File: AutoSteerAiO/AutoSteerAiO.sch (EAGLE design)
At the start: 82 parts, among them J4 CONNECTOR 1x5 PINS, K4 CB1A-P-12V, U1 VX7805-1000

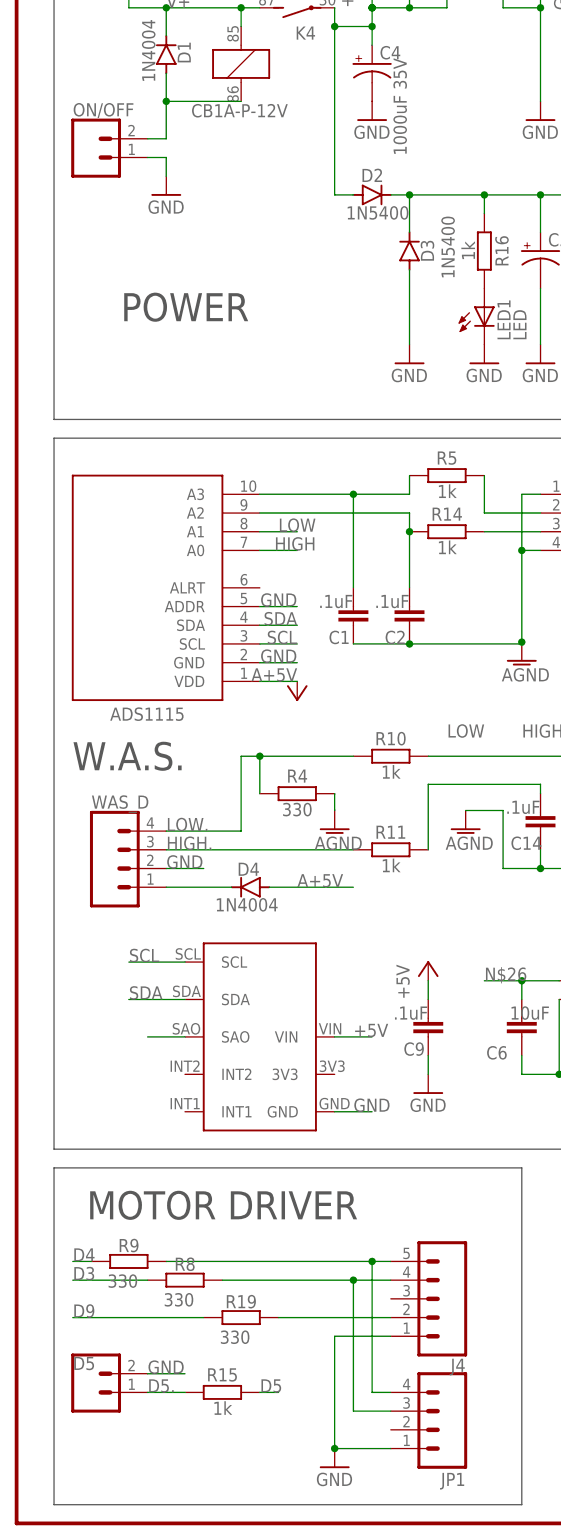
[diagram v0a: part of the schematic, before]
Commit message: Add files via upload
added led autosteer
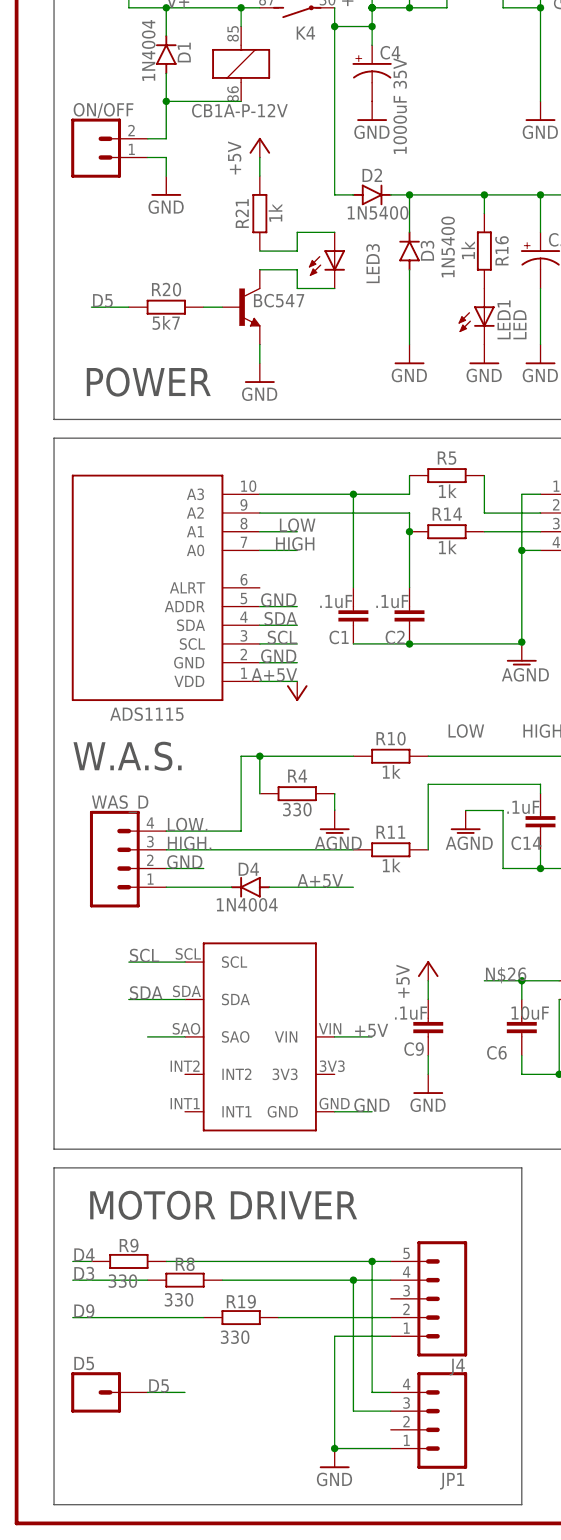
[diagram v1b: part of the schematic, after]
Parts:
- removed R15: 1k, resistor:R-EU_0207/7
- added LED3: LED, adafruit:LED5MM
- added R20: 5k7, resistor:R-EU_0207/7
- added R21: 1k, resistor:R-EU_0207/7
- added T1: BC547, transistor:BC547
- D5: device SparkFun-Connectors:CONN_02 -> SparkFun-Connectors:CONN_01
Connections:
- removed net D5.: D5.1, R15.1
- new net N$23: R20.2, T1.B
- new net N$24: LED3.A, R21.1
- new net N$27: LED3.C, T1.C
- net +5V: now also R21.2
- net D5: now also D5.1, R20.1; no longer R15.2
- net GND: now also T1.E; no longer D5.2
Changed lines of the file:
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@@
 <attribute name="OC_NEWARK" value="unknown"/>
 </part>
-<part name="D5" library="SparkFun-Connectors" library_urn="urn:adsk.eagle:library:513" deviceset="CONN_02" device="" package3d_urn="urn:adsk.eagle:package:38039/1" value="CONNECTOR 1x1 PIN">
+<part name="D5" library="SparkFun-Connectors" library_urn="urn:adsk.eagle:library:513" deviceset="CONN_01" device="" package3d_urn="urn:adsk.eagle:package:38028/1" value="CONNECTOR 1x1 PIN">
 <attribute name="MF" value=""/>
 <attribute name="MPN" value=""/>
@@
 </part>
 <part name="U$13" library="#MMA8542Q" deviceset="MMA8542Q" device=""/>
-<part name="R15" library="resistor" library_urn="urn:adsk.eagle:library:348" deviceset="R-EU_" device="0207/7" package3d_urn="urn:adsk.eagle:package:23493/2" value="1k">
+<part name="T1" library="transistor" library_urn="urn:adsk.eagle:library:402" deviceset="BC547" device="" package3d_urn="urn:adsk.eagle:package:28523/2"/>
+<part name="R20" library="resistor" library_urn="urn:adsk.eagle:library:348" deviceset="R-EU_" device="0207/7" package3d_urn="urn:adsk.eagle:package:23493/2" value="5k7">
+<attribute name="MF" value=""/>
+<attribute name="MPN" value=""/>
+<attribute name="OC_NEWARK" value="unknown"/>
+</part>
+<part name="R21" library="resistor" library_urn="urn:adsk.eagle:library:348" deviceset="R-EU_" device="0207/7" package3d_urn="urn:adsk.eagle:package:23493/2" value="1k">
+<attribute name="MF" value=""/>
+<attribute name="MPN" value=""/>
+<attribute name="OC_NEWARK" value="unknown"/>
+</part>
+<part name="P+3" library="supply1" library_urn="urn:adsk.eagle:library:371" deviceset="+5V" device=""/>
+<part name="GND11" library="supply1" library_urn="urn:adsk.eagle:library:371" deviceset="GND" device=""/>
+<part name="LED3" library="adafruit" library_urn="urn:adsk.eagle:library:420" deviceset="LED" device="5MM" package3d_urn="urn:adsk.eagle:package:6240538/1" value="LED">
 <attribute name="MF" value=""/>
 <attribute name="MPN" value=""/>
@@
 <wire x1="144.78" y1="213.36" x2="144.78" y2="284.48" width="0.1524" layer="97"/>
 <wire x1="144.78" y1="213.36" x2="5.08" y2="213.36" width="0.1524" layer="97"/>
-<text x="22.86" y="228.6" size="3.81" layer="97" font="vector" align="center">POWER</text>
+<text x="17.78" y="218.44" size="3.81" layer="97" font="vector" align="center">POWER</text>
 <wire x1="147.32" y1="198.12" x2="147.32" y2="256.54" width="0.1524" layer="97"/>
 <wire x1="205.74" y1="198.12" x2="147.32" y2="198.12" width="0.1524" layer="97"/>
@@
 </instance>
 <instance part="U$13" gate="G$1" x="86.36" y="149.86" smashed="yes"/>
-<instance part="R15" gate="G$1" x="27.94" y="81.28" smashed="yes">
-<attribute name="NAME" x="27.94" y="82.7786" size="1.778" layer="95" rot="R180" align="top-center"/>
-<attribute name="VALUE" x="27.94" y="80.01" size="1.778" layer="95" rot="R180" align="bottom-center"/>
-<attribute name="OC_NEWARK" x="27.94" y="81.28" size="1.778" layer="96" display="off"/>
-<attribute name="MF" x="27.94" y="81.28" size="1.778" layer="96" display="off"/>
-<attribute name="MPN" x="27.94" y="81.28" size="1.778" layer="96" display="off"/>
+<instance part="T1" gate="G$1" x="30.48" y="228.6" smashed="yes">
+<attribute name="VALUE" x="32.004" y="228.6" size="1.778" layer="96"/>
+</instance>
+<instance part="R20" gate="G$1" x="20.32" y="228.6" smashed="yes">
+<attribute name="NAME" x="20.32" y="230.0986" size="1.778" layer="95" rot="R180" align="top-center"/>
+<attribute name="VALUE" x="20.32" y="227.33" size="1.778" layer="95" rot="R180" align="bottom-center"/>
+<attribute name="OC_NEWARK" x="20.32" y="228.6" size="1.778" layer="96" display="off"/>
+<attribute name="MF" x="20.32" y="228.6" size="1.778" layer="96" display="off"/>
+<attribute name="MPN" x="20.32" y="228.6" size="1.778" layer="96" display="off"/>
+</instance>
+<instance part="R21" gate="G$1" x="33.02" y="241.3" smashed="yes" rot="R90">
+<attribute name="NAME" x="31.5214" y="241.3" size="1.778" layer="95" rot="R270" align="top-center"/>
+<attribute name="VALUE" x="34.29" y="241.3" size="1.778" layer="95" rot="R270" align="bottom-center"/>
+<attribute name="OC_NEWARK" x="33.02" y="241.3" size="1.778" layer="96" rot="R90" display="off"/>
+<attribute name="MF" x="33.02" y="241.3" size="1.778" layer="96" rot="R90" display="off"/>
+<attribute name="MPN" x="33.02" y="241.3" size="1.778" layer="96" rot="R90" display="off"/>
+</instance>
+<instance part="P+3" gate="1" x="33.02" y="251.46" smashed="yes">
+<attribute name="VALUE" x="30.48" y="246.38" size="1.778" layer="96" rot="R90"/>
+</instance>
+<instance part="GND11" gate="1" x="33.02" y="218.44" smashed="yes">
+<attribute name="VALUE" x="30.48" y="215.9" size="1.778" layer="96"/>
+</instance>
+<instance part="LED3" gate="G$1" x="43.18" y="236.22" smashed="yes">
+<attribute name="NAME" x="49.276" y="231.648" size="1.778" layer="95" rot="R90"/>
+<attribute name="OC_NEWARK" x="43.18" y="236.22" size="1.778" layer="96" display="off"/>
+<attribute name="MF" x="43.18" y="236.22" size="1.778" layer="96" display="off"/>
+<attribute name="MPN" x="43.18" y="236.22" size="1.778" layer="96" display="off"/>
 </instance>
 </instances>
@@
 <pinref part="P+5" gate="1" pin="+5V"/>
 <wire x1="55.88" y1="134.62" x2="55.88" y2="137.16" width="0.1524" layer="91"/>
+</segment>
+<segment>
+<pinref part="R21" gate="G$1" pin="2"/>
+<pinref part="P+3" gate="1" pin="+5V"/>
+<wire x1="33.02" y1="248.92" x2="33.02" y2="246.38" width="0.1524" layer="91"/>
 </segment>
 </net>
@@
 </segment>
 <segment>
-<pinref part="D5" gate="G$1" pin="2"/>
-<wire x1="17.78" y1="83.82" x2="22.86" y2="83.82" width="0.1524" layer="91"/>
-<label x="17.78" y="83.82" size="1.778" layer="95"/>
-</segment>
-<segment>
 <pinref part="0" gate="J$1" pin="3"/>
 <wire x1="177.8" y1="279.4" x2="180.34" y2="279.4" width="0.1524" layer="91"/>
@@
 <label x="160.02" y="274.32" size="1.778" layer="95"/>
 </segment>
+<segment>
+<pinref part="T1" gate="G$1" pin="E"/>
+<pinref part="GND11" gate="1" pin="GND"/>
+<wire x1="33.02" y1="220.98" x2="33.02" y2="223.52" width="0.1524" layer="91"/>
+</segment>
 </net>
 <net name="D5" class="0">
@@
 </segment>
 <segment>
-<pinref part="R15" gate="G$1" pin="2"/>
-<wire x1="33.02" y1="81.28" x2="35.56" y2="81.28" width="0.1524" layer="91"/>
-<label x="33.02" y="81.28" size="1.778" layer="95"/>
+<pinref part="R20" gate="G$1" pin="1"/>
+<wire x1="15.24" y1="228.6" x2="10.16" y2="228.6" width="0.1524" layer="91"/>
+<label x="10.16" y="228.6" size="1.778" layer="95"/>
+</segment>
+<segment>
+<pinref part="D5" gate="G$1" pin="1"/>
+<wire x1="17.78" y1="81.28" x2="22.86" y2="81.28" width="0.1524" layer="91"/>
+<label x="17.78" y="81.28" size="1.778" layer="95"/>
 </segment>
 </net>
@@
 </segment>
 </net>
-<net name="D5." class="0">
-<segment>
-<pinref part="D5" gate="G$1" pin="1"/>
-<wire x1="17.78" y1="81.28" x2="22.86" y2="81.28" width="0.1524" layer="91"/>
-<label x="17.78" y="81.28" size="1.778" layer="95"/>
-<pinref part="R15" gate="G$1" pin="1"/>
-</segment>
-</net>
 <net name="SAO" class="0">
 <segment>
@@
 </segment>
 </net>
+<net name="N$23" class="0">
+<segment>
+<pinref part="T1" gate="G$1" pin="B"/>
+<pinref part="R20" gate="G$1" pin="2"/>
+<wire x1="25.4" y1="228.6" x2="27.94" y2="228.6" width="0.1524" layer="91"/>
+</segment>
+</net>
+<net name="N$24" class="0">
+<segment>
+<pinref part="LED3" gate="G$1" pin="A"/>
+<wire x1="43.18" y1="238.76" x2="38.1" y2="238.76" width="0.1524" layer="91"/>
+<wire x1="38.1" y1="238.76" x2="38.1" y2="236.22" width="0.1524" layer="91"/>
+<pinref part="R21" gate="G$1" pin="1"/>
+<wire x1="38.1" y1="236.22" x2="33.02" y2="236.22" width="0.1524" layer="91"/>
+</segment>
+</net>
+<net name="N$27" class="0">
+<segment>
+<pinref part="T1" gate="G$1" pin="C"/>
+<wire x1="33.02" y1="233.68" x2="38.1" y2="233.68" width="0.1524" layer="91"/>
+<wire x1="38.1" y1="233.68" x2="38.1" y2="231.14" width="0.1524" layer="91"/>
+<pinref part="LED3" gate="G$1" pin="C"/>
+<wire x1="38.1" y1="231.14" x2="43.18" y2="231.14" width="0.1524" layer="91"/>
+</segment>
+</net>

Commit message: Add files via upload
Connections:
- net N$25: now also R16.1
- net N$26: no longer R16.1
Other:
- moved on the sheet: C6, C7, C8, L1, LED1, R16

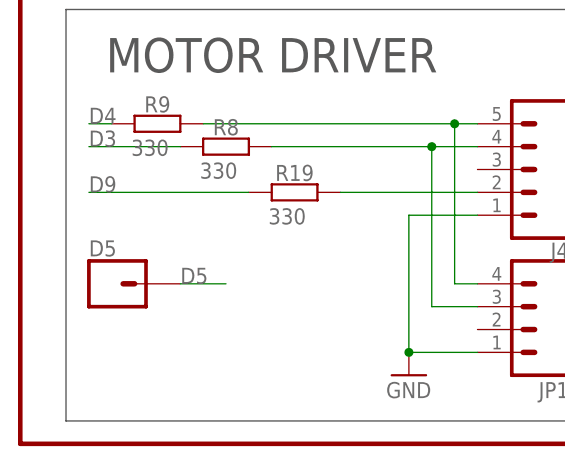
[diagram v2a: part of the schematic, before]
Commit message: Add files via upload
Adeed 5V connector for IBT2
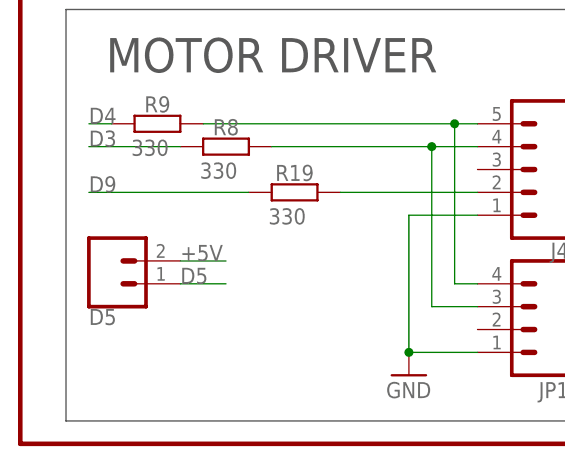
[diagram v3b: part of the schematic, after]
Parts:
- D5: device SparkFun-Connectors:CONN_01 -> SparkFun-Connectors:CONN_02
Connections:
- net +5V: now also D5.2
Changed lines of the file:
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@@
 <attribute name="OC_NEWARK" value="unknown"/>
 </part>
-<part name="D5" library="SparkFun-Connectors" library_urn="urn:adsk.eagle:library:513" deviceset="CONN_01" device="" package3d_urn="urn:adsk.eagle:package:38028/1" value="CONNECTOR 1x1 PIN">
+<part name="D5" library="SparkFun-Connectors" library_urn="urn:adsk.eagle:library:513" deviceset="CONN_02" device="" package3d_urn="urn:adsk.eagle:package:38039/1" value="CONNECTOR 1x1 PIN">
 <attribute name="MF" value=""/>
 <attribute name="MPN" value=""/>
@@
 </instance>
 <instance part="D5" gate="G$1" x="10.16" y="81.28" smashed="yes">
-<attribute name="NAME" x="7.62" y="84.328" size="1.778" layer="95" font="vector"/>
+<attribute name="NAME" x="7.62" y="76.708" size="1.778" layer="95" font="vector"/>
 <attribute name="OC_NEWARK" x="10.16" y="81.28" size="1.778" layer="96" rot="R90" display="off"/>
 <attribute name="MF" x="10.16" y="81.28" size="1.778" layer="96" rot="R90" display="off"/>
@@
 <wire x1="33.02" y1="248.92" x2="33.02" y2="246.38" width="0.1524" layer="91"/>
 </segment>
+<segment>
+<pinref part="D5" gate="G$1" pin="2"/>
+<wire x1="17.78" y1="83.82" x2="22.86" y2="83.82" width="0.1524" layer="91"/>
+<label x="17.78" y="83.82" size="1.778" layer="95"/>
+</segment>
 </net>

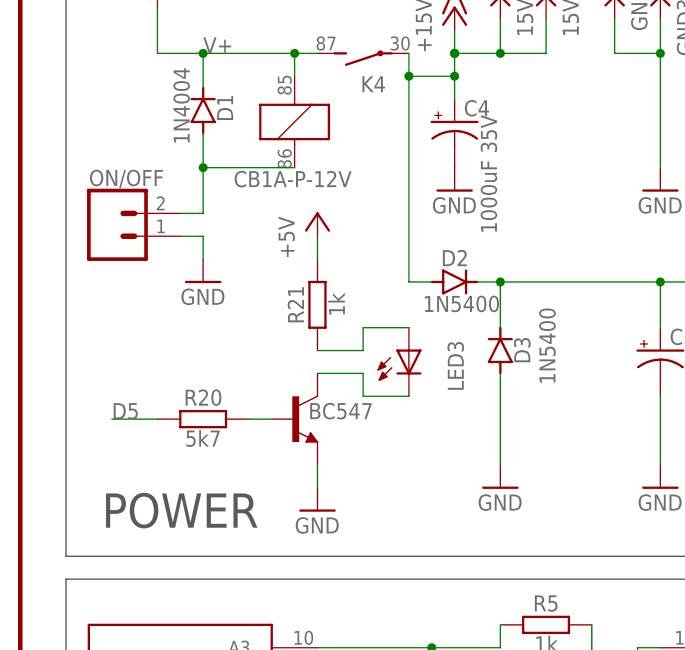
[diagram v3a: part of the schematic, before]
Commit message: Add files via upload
Added diode D6 to protect from reverse polarity
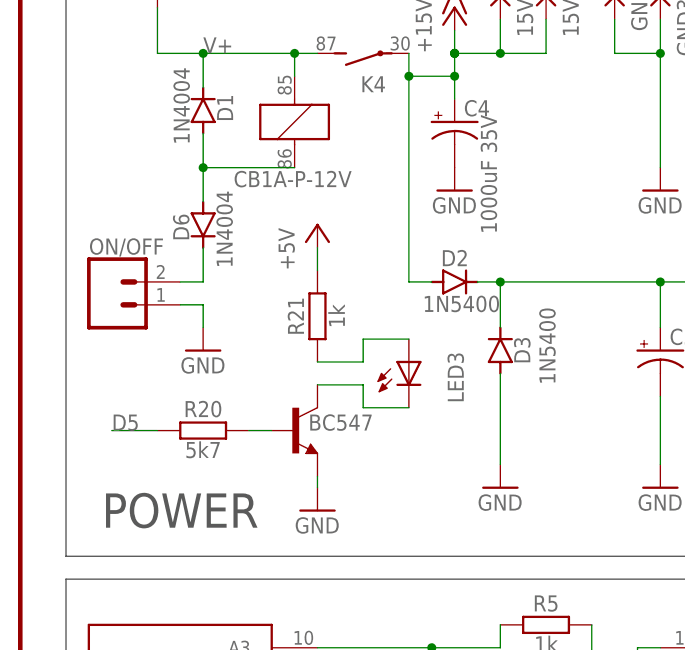
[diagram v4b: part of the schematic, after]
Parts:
- added D6: 1N4004, diode:1N4004
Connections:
- new net N$28: D6.C, ON/OFF.2
- net N$5: now also D6.A; no longer ON/OFF.2
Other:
- moved on the sheet: LED3, ON/OFF, R20, R21
